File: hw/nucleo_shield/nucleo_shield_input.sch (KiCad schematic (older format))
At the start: 38 parts, among them P1 CONN_01X10, P5 CONN_01X10, U3 LTV-847, U4 LTV-847, U5 LTV-847, U6 LTV-847

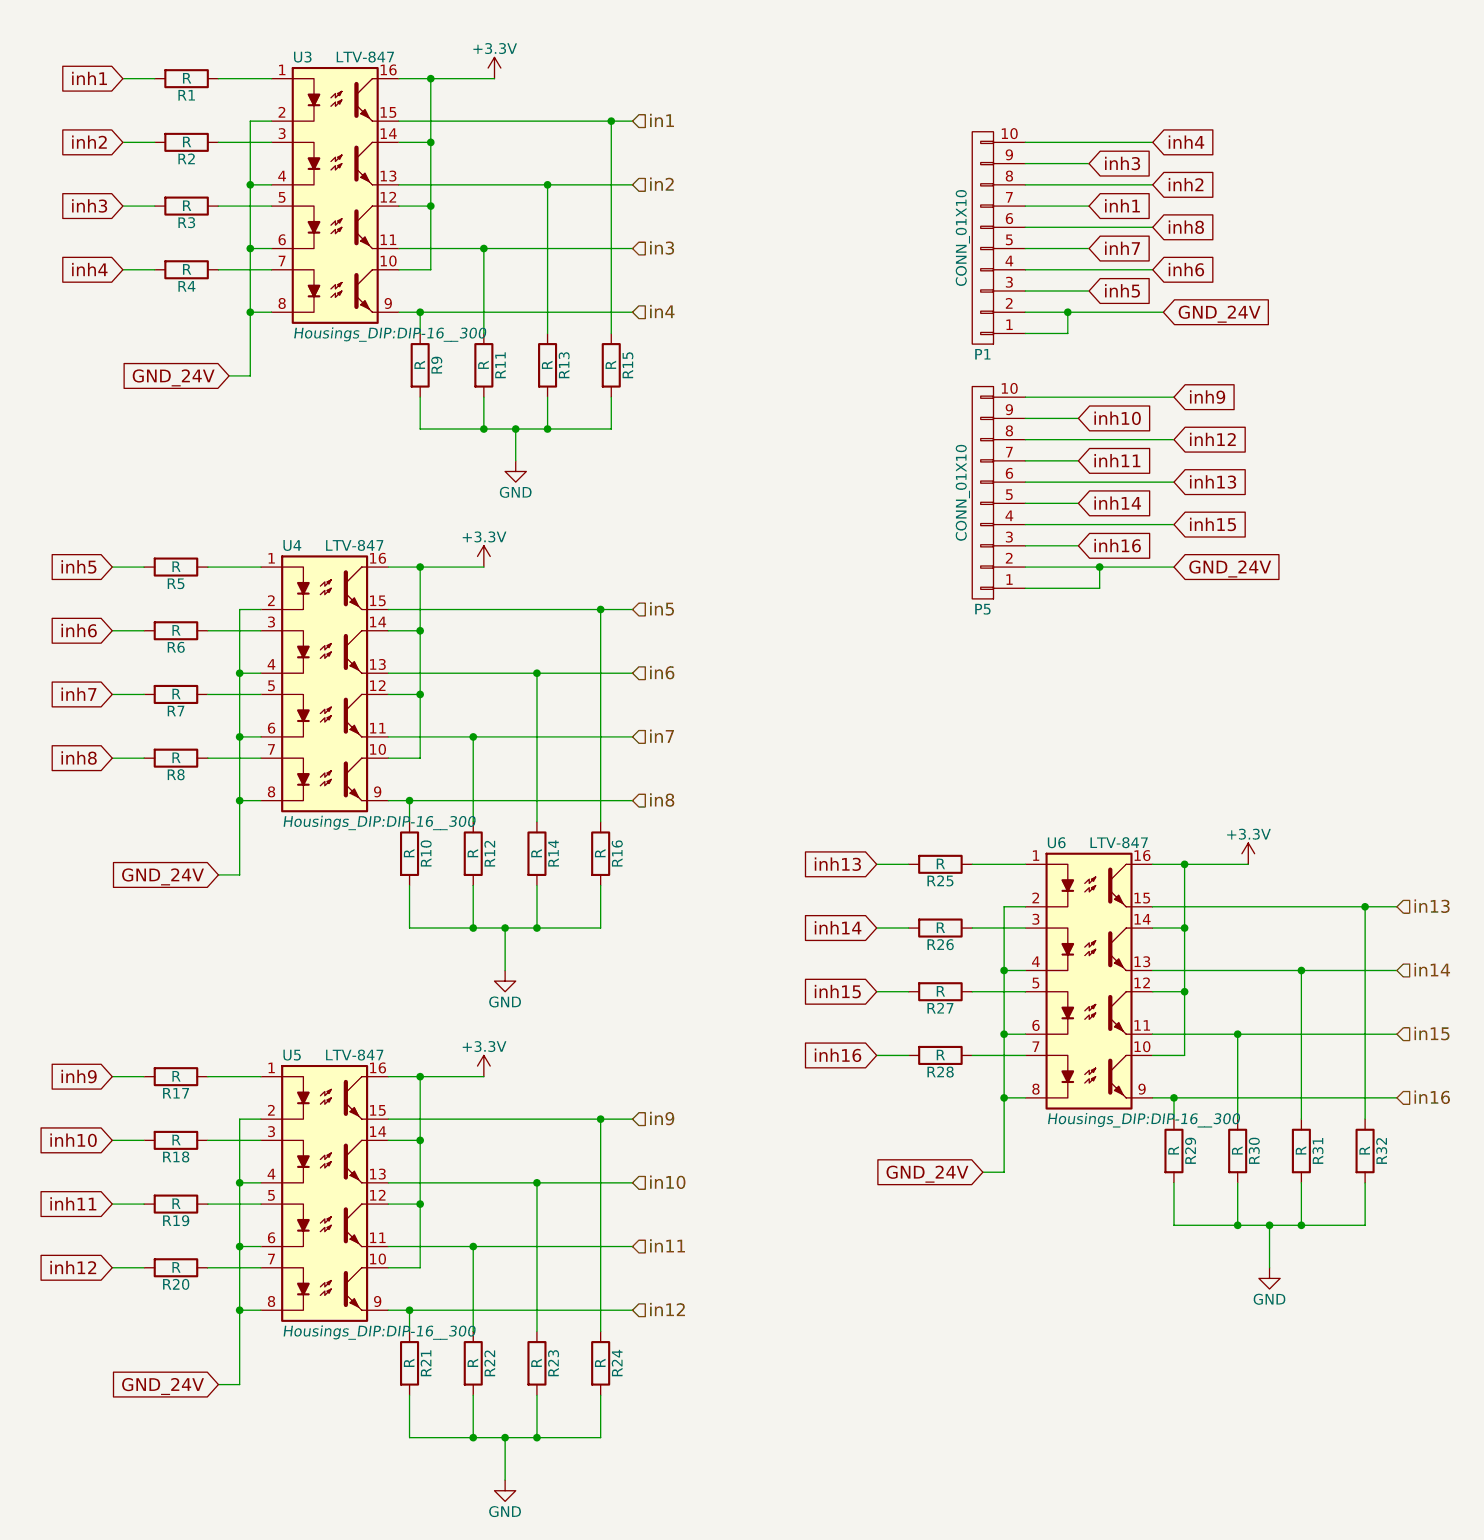
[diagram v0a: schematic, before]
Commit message: Update schematic to add sct and io expander
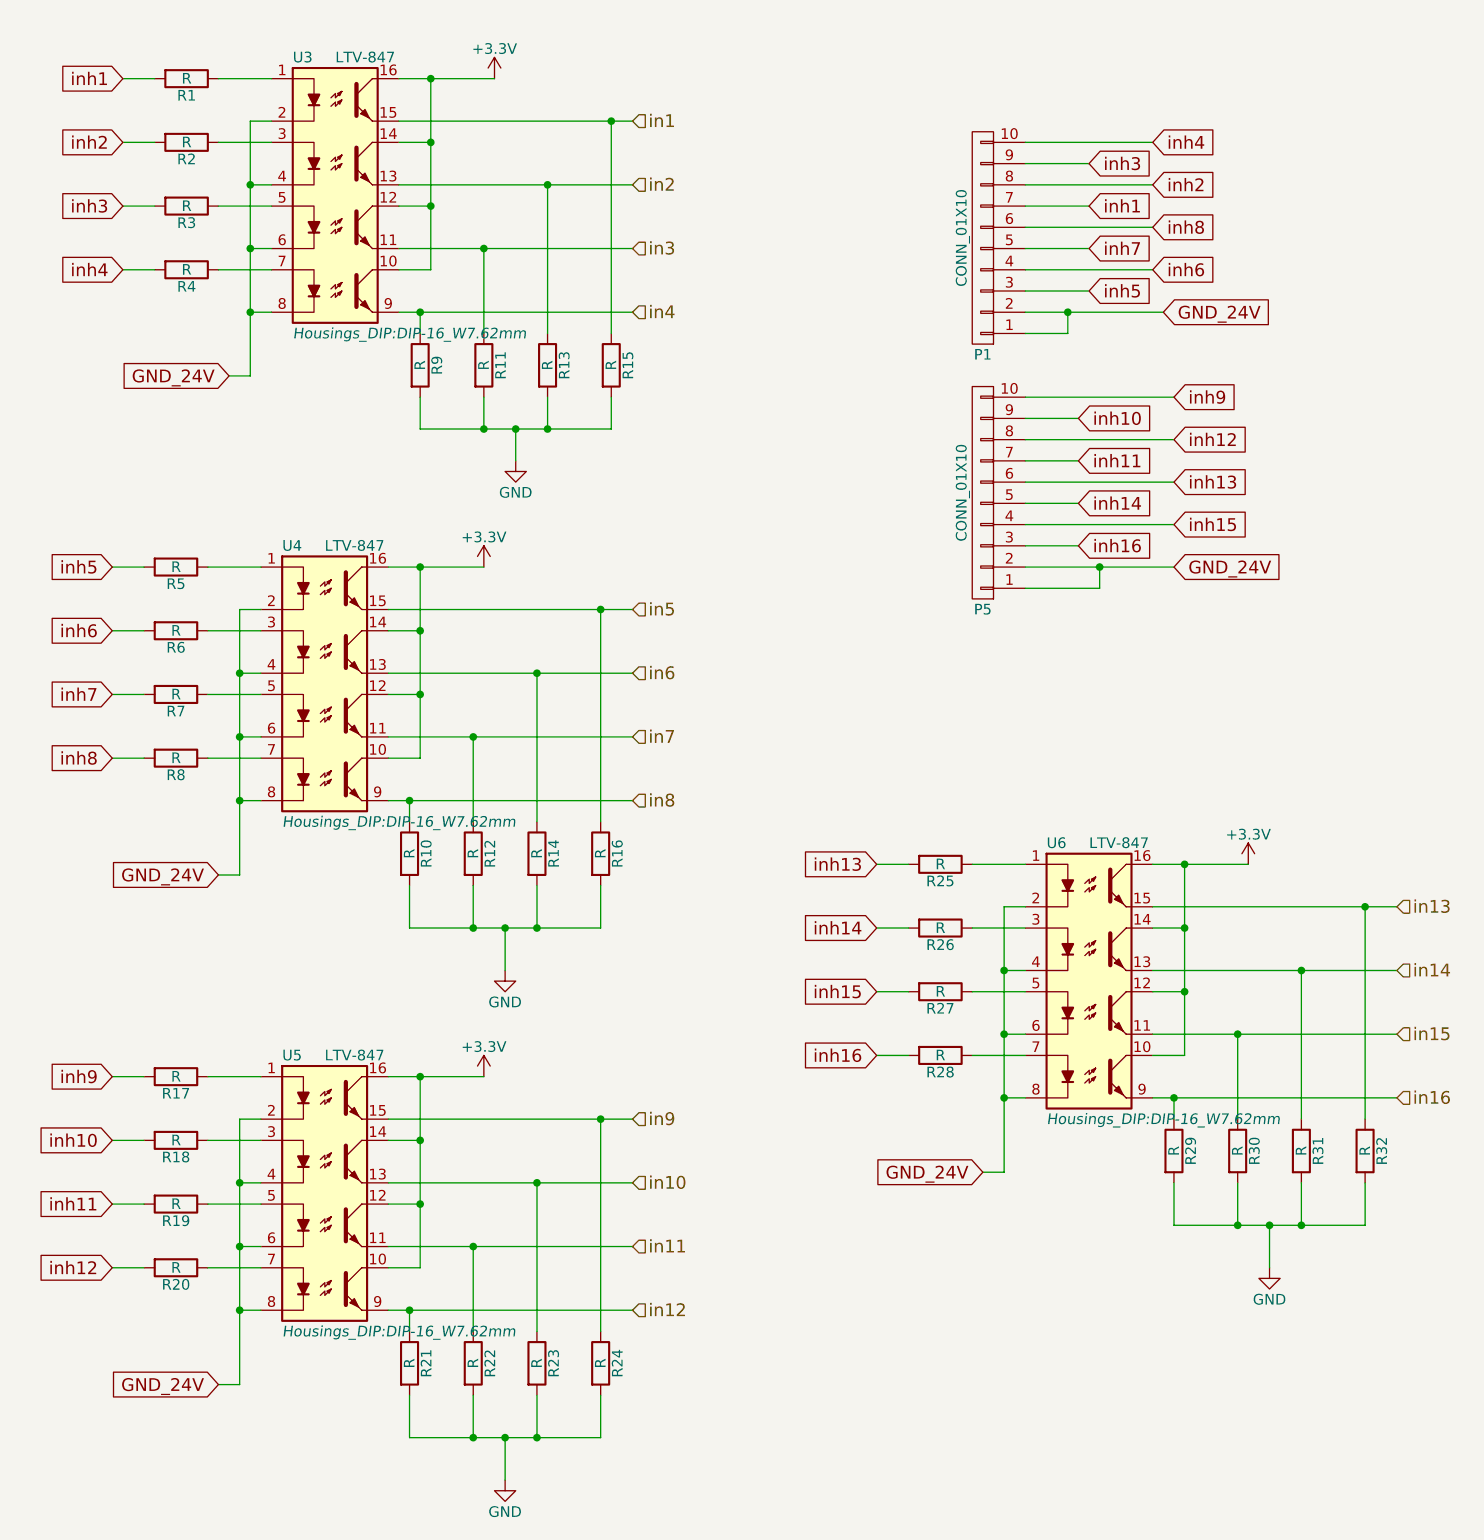
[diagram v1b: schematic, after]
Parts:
- U3, U4, U5, U6: footprint Housings_DIP:DIP-16__300 -> Housings_DIP:DIP-16_W7.62mm
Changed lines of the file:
@@
 LIBS:memory
 LIBS:xilinx
-LIBS:special
 LIBS:microcontrollers
 LIBS:dsp
@@
 $Descr A4 11693 8268
 encoding utf-8
-Sheet 3 4
+Sheet 4 4
 Title ""
 Date ""
@@
 F 0 "U3" H 2200 2100 50  0000 L CNN
 F 1 "LTV-847" H 2400 2100 50  0000 L CNN
-F 2 "Housings_DIP:DIP-16__300" H 2200 800 50  0000 L CIN
+F 2 "Housings_DIP:DIP-16_W7.62mm" H 2200 800 50  0000 L CIN
 F 3 "" H 2400 1300 50  0000 L CNN
 	1    2400 1400
@@
 $EndComp
 $Comp
-L GND #PWR022
+L GND #PWR038
 U 1 1 5728E40C
 P 3200 5000
-F 0 "#PWR022" H 3200 4750 50  0001 C CNN
+F 0 "#PWR038" H 3200 4750 50  0001 C CNN
 F 1 "GND" H 3200 4850 50  0000 C CNN
 F 2 "" H 3200 5000 60  0000 C CNN
@@
 $EndComp
 $Comp
-L GND #PWR023
+L GND #PWR039
 U 1 1 5728E412
 P 3250 2600
-F 0 "#PWR023" H 3250 2350 50  0001 C CNN
+F 0 "#PWR039" H 3250 2350 50  0001 C CNN
 F 1 "GND" H 3250 2450 50  0000 C CNN
 F 2 "" H 3250 2600 60  0000 C CNN
@@
 F 0 "U4" H 2150 4400 50  0000 L CNN
 F 1 "LTV-847" H 2350 4400 50  0000 L CNN
-F 2 "Housings_DIP:DIP-16__300" H 2150 3100 50  0000 L CIN
+F 2 "Housings_DIP:DIP-16_W7.62mm" H 2150 3100 50  0000 L CIN
 F 3 "" H 2350 3600 50  0000 L CNN
 	1    2350 3700
@@
 	1950 4550 1850 4550
 $Comp
-L +3.3V #PWR024
+L +3.3V #PWR040
 U 1 1 5728E4BD
 P 3100 3100
-F 0 "#PWR024" H 3100 2950 50  0001 C CNN
+F 0 "#PWR040" H 3100 2950 50  0001 C CNN
 F 1 "+3.3V" H 3100 3240 50  0000 C CNN
 F 2 "" H 3100 3100 60  0000 C CNN
@@
 $EndComp
 $Comp
-L +3.3V #PWR025
+L +3.3V #PWR041
 U 1 1 5728E4C3
 P 3150 800
-F 0 "#PWR025" H 3150 650 50  0001 C CNN
+F 0 "#PWR041" H 3150 650 50  0001 C CNN
 F 1 "+3.3V" H 3150 940 50  0000 C CNN
 F 2 "" H 3150 800 60  0000 C CNN
@@
 $EndComp
 $Comp
-L GND #PWR026
+L GND #PWR042
 U 1 1 5728E4E9
 P 3200 7400
-F 0 "#PWR026" H 3200 7150 50  0001 C CNN
+F 0 "#PWR042" H 3200 7150 50  0001 C CNN
 F 1 "GND" H 3200 7250 50  0000 C CNN
 F 2 "" H 3200 7400 60  0000 C CNN
@@
 F 0 "U5" H 2150 6800 50  0000 L CNN
 F 1 "LTV-847" H 2350 6800 50  0000 L CNN
-F 2 "Housings_DIP:DIP-16__300" H 2150 5500 50  0000 L CIN
+F 2 "Housings_DIP:DIP-16_W7.62mm" H 2150 5500 50  0000 L CIN
 F 3 "" H 2350 6000 50  0000 L CNN
 	1    2350 6100
@@
 	1950 6950 1850 6950
 $Comp
-L +3.3V #PWR027
+L +3.3V #PWR043
 U 1 1 5728E545
 P 3100 5500
-F 0 "#PWR027" H 3100 5350 50  0001 C CNN
+F 0 "#PWR043" H 3100 5350 50  0001 C CNN
 F 1 "+3.3V" H 3100 5640 50  0000 C CNN
 F 2 "" H 3100 5500 60  0000 C CNN
@@
 $EndComp
 $Comp
-L GND #PWR028
+L GND #PWR044
 U 1 1 572A109B
 P 6800 6400
-F 0 "#PWR028" H 6800 6150 50  0001 C CNN
+F 0 "#PWR044" H 6800 6150 50  0001 C CNN
 F 1 "GND" H 6800 6250 50  0000 C CNN
 F 2 "" H 6800 6400 60  0000 C CNN
@@
 F 0 "U6" H 5750 5800 50  0000 L CNN
 F 1 "LTV-847" H 5950 5800 50  0000 L CNN
-F 2 "Housings_DIP:DIP-16__300" H 5750 4500 50  0000 L CIN
+F 2 "Housings_DIP:DIP-16_W7.62mm" H 5750 4500 50  0000 L CIN
 F 3 "" H 5950 5000 50  0000 L CNN
 	1    5950 5100
@@
 	5550 5950 5450 5950
 $Comp
-L +3.3V #PWR029
+L +3.3V #PWR045
 U 1 1 572A10F2
 P 6700 4500
-F 0 "#PWR029" H 6700 4350 50  0001 C CNN
+F 0 "#PWR045" H 6700 4350 50  0001 C CNN
 F 1 "+3.3V" H 6700 4640 50  0000 C CNN
 F 2 "" H 6700 4500 60  0000 C CNN

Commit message: Hw: add intermediate header between output and ULN2803
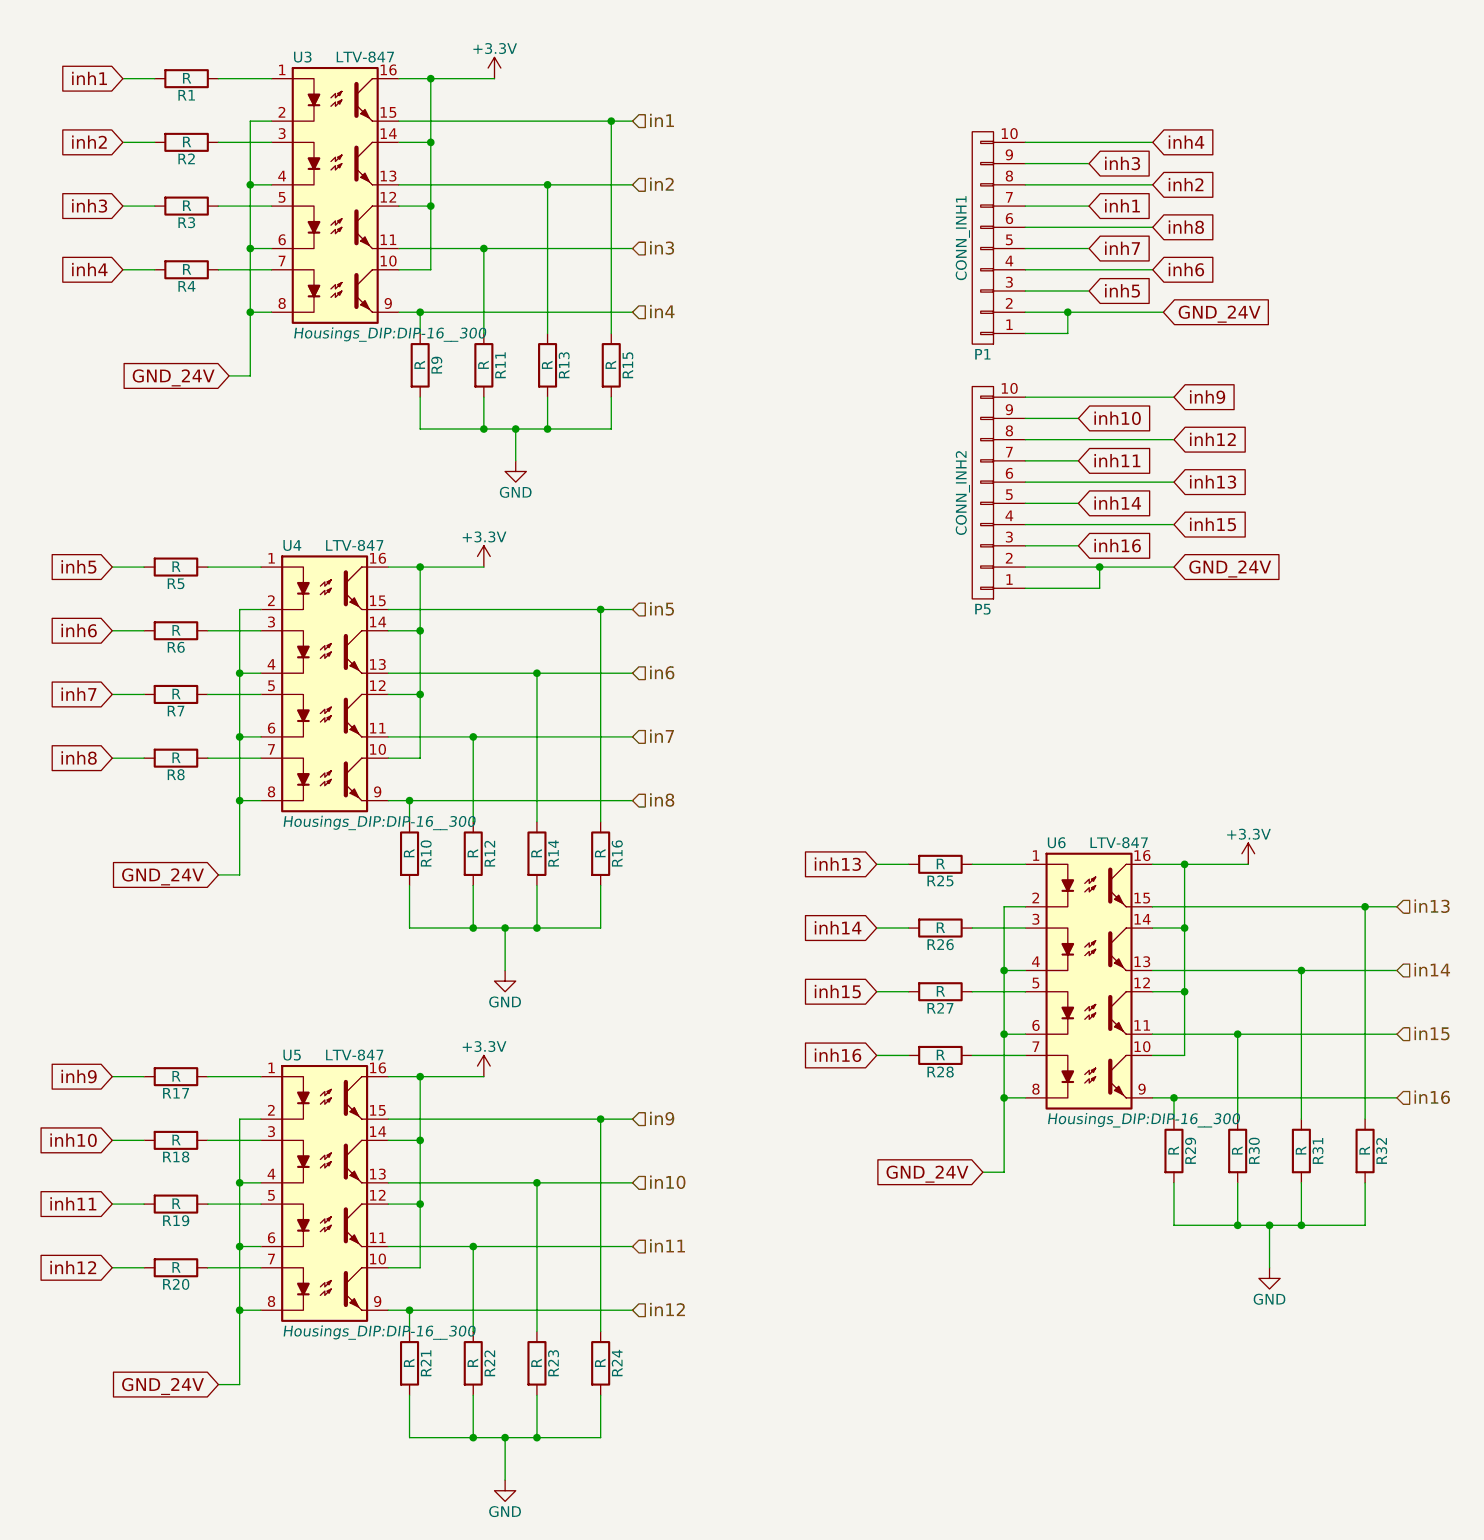
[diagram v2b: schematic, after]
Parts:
- P1: value CONN_01X10 -> CONN_INH1
- P5: value CONN_01X10 -> CONN_INH2
- U3, U4, U5, U6: footprint Housings_DIP:DIP-16_W7.62mm -> Housings_DIP:DIP-16__300
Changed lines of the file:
@@
 LIBS:memory
 LIBS:xilinx
+LIBS:special
 LIBS:microcontrollers
 LIBS:dsp
@@
 LIBS:valves
 LIBS:F411RE
+LIBS:w_analog
 LIBS:nucleo_shield-cache
 EELAYER 25 0
@@
 F 0 "U3" H 2200 2100 50  0000 L CNN
 F 1 "LTV-847" H 2400 2100 50  0000 L CNN
-F 2 "Housings_DIP:DIP-16_W7.62mm" H 2200 800 50  0000 L CIN
+F 2 "Housings_DIP:DIP-16__300" H 2200 800 50  0000 L CIN
 F 3 "" H 2400 1300 50  0000 L CNN
 	1    2400 1400
@@
 $EndComp
 $Comp
-L GND #PWR038
+L GND #PWR046
 U 1 1 5728E40C
 P 3200 5000
-F 0 "#PWR038" H 3200 4750 50  0001 C CNN
+F 0 "#PWR046" H 3200 4750 50  0001 C CNN
 F 1 "GND" H 3200 4850 50  0000 C CNN
 F 2 "" H 3200 5000 60  0000 C CNN
@@
 $EndComp
 $Comp
-L GND #PWR039
+L GND #PWR047
 U 1 1 5728E412
 P 3250 2600
-F 0 "#PWR039" H 3250 2350 50  0001 C CNN
+F 0 "#PWR047" H 3250 2350 50  0001 C CNN
 F 1 "GND" H 3250 2450 50  0000 C CNN
 F 2 "" H 3250 2600 60  0000 C CNN
@@
 F 0 "U4" H 2150 4400 50  0000 L CNN
 F 1 "LTV-847" H 2350 4400 50  0000 L CNN
-F 2 "Housings_DIP:DIP-16_W7.62mm" H 2150 3100 50  0000 L CIN
+F 2 "Housings_DIP:DIP-16__300" H 2150 3100 50  0000 L CIN
 F 3 "" H 2350 3600 50  0000 L CNN
 	1    2350 3700
@@
 	1950 4550 1850 4550
 $Comp
-L +3.3V #PWR040
+L +3.3V #PWR048
 U 1 1 5728E4BD
 P 3100 3100
-F 0 "#PWR040" H 3100 2950 50  0001 C CNN
+F 0 "#PWR048" H 3100 2950 50  0001 C CNN
 F 1 "+3.3V" H 3100 3240 50  0000 C CNN
 F 2 "" H 3100 3100 60  0000 C CNN
@@
 $EndComp
 $Comp
-L +3.3V #PWR041
+L +3.3V #PWR049
 U 1 1 5728E4C3
 P 3150 800
-F 0 "#PWR041" H 3150 650 50  0001 C CNN
+F 0 "#PWR049" H 3150 650 50  0001 C CNN
 F 1 "+3.3V" H 3150 940 50  0000 C CNN
 F 2 "" H 3150 800 60  0000 C CNN
@@
 $EndComp
 $Comp
-L GND #PWR042
+L GND #PWR050
 U 1 1 5728E4E9
 P 3200 7400
-F 0 "#PWR042" H 3200 7150 50  0001 C CNN
+F 0 "#PWR050" H 3200 7150 50  0001 C CNN
 F 1 "GND" H 3200 7250 50  0000 C CNN
 F 2 "" H 3200 7400 60  0000 C CNN
@@
 F 0 "U5" H 2150 6800 50  0000 L CNN
 F 1 "LTV-847" H 2350 6800 50  0000 L CNN
-F 2 "Housings_DIP:DIP-16_W7.62mm" H 2150 5500 50  0000 L CIN
+F 2 "Housings_DIP:DIP-16__300" H 2150 5500 50  0000 L CIN
 F 3 "" H 2350 6000 50  0000 L CNN
 	1    2350 6100
@@
 	1950 6950 1850 6950
 $Comp
-L +3.3V #PWR043
+L +3.3V #PWR051
 U 1 1 5728E545
 P 3100 5500
-F 0 "#PWR043" H 3100 5350 50  0001 C CNN
+F 0 "#PWR051" H 3100 5350 50  0001 C CNN
 F 1 "+3.3V" H 3100 5640 50  0000 C CNN
 F 2 "" H 3100 5500 60  0000 C CNN
@@
 P 5450 1550
 F 0 "P1" H 5450 2100 50  0000 C CNN
-F 1 "CONN_01X10" V 5550 1550 50  0000 C CNN
+F 1 "CONN_INH1" V 5550 1550 50  0000 C CNN
 F 2 "w_conn_screw:mors_10p" H 5450 1550 60  0001 C CNN
 F 3 "" H 5450 1550 60  0000 C CNN
@@
 P 5450 2750
 F 0 "P5" H 5450 3300 50  0000 C CNN
-F 1 "CONN_01X10" V 5550 2750 50  0000 C CNN
+F 1 "CONN_INH2" V 5550 2750 50  0000 C CNN
 F 2 "w_conn_screw:mors_10p" H 5450 2750 60  0001 C CNN
 F 3 "" H 5450 2750 60  0000 C CNN
@@
 $EndComp
 $Comp
-L GND #PWR044
+L GND #PWR052
 U 1 1 572A109B
 P 6800 6400
-F 0 "#PWR044" H 6800 6150 50  0001 C CNN
+F 0 "#PWR052" H 6800 6150 50  0001 C CNN
 F 1 "GND" H 6800 6250 50  0000 C CNN
 F 2 "" H 6800 6400 60  0000 C CNN
@@
 F 0 "U6" H 5750 5800 50  0000 L CNN
 F 1 "LTV-847" H 5950 5800 50  0000 L CNN
-F 2 "Housings_DIP:DIP-16_W7.62mm" H 5750 4500 50  0000 L CIN
+F 2 "Housings_DIP:DIP-16__300" H 5750 4500 50  0000 L CIN
 F 3 "" H 5950 5000 50  0000 L CNN
 	1    5950 5100
@@
 	5550 5950 5450 5950
 $Comp
-L +3.3V #PWR045
+L +3.3V #PWR053
 U 1 1 572A10F2
 P 6700 4500
-F 0 "#PWR045" H 6700 4350 50  0001 C CNN
+F 0 "#PWR053" H 6700 4350 50  0001 C CNN
 F 1 "+3.3V" H 6700 4640 50  0000 C CNN
 F 2 "" H 6700 4500 60  0000 C CNN

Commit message: HW: fix a lot of connection and start positionning
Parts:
- removed R10, R11, R12, R13, R14, R15, R16, R21, R22, R23, R24, R29, R30, R31, R32, R9: R, Resistors_ThroughHole:Resistor_Horizontal_RM10mm, symbol R
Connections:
- net inh10: now also R19.2; no longer R18.2
- net inh11: now also R17.2; no longer R19.2
- net inh12: now also R18.2; no longer R20.2
- net inh13: now also R28.2; no longer R25.2
- net inh14: now also R27.2; no longer R26.2
- net inh15: now also R26.2; no longer R27.2
- net inh16: now also R25.2; no longer R28.2
- net inh9: now also R20.2; no longer R17.2
